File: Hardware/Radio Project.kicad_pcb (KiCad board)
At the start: 10 copper layers, 100 x 70 mm, 88 parts, among them J1 132225, J2 132225, J3 USB_C_Receptacle, J4 FTSH-105-X-X-DV-007-P-X, J5 WE-RJ45_7499010211A, SW1 208-4, U1 STM32F407VGT6, U2 ADP2164ACPZ-3.3-R7, U3 Si4464, U4 Si4464, U5 DP83822IRHBR

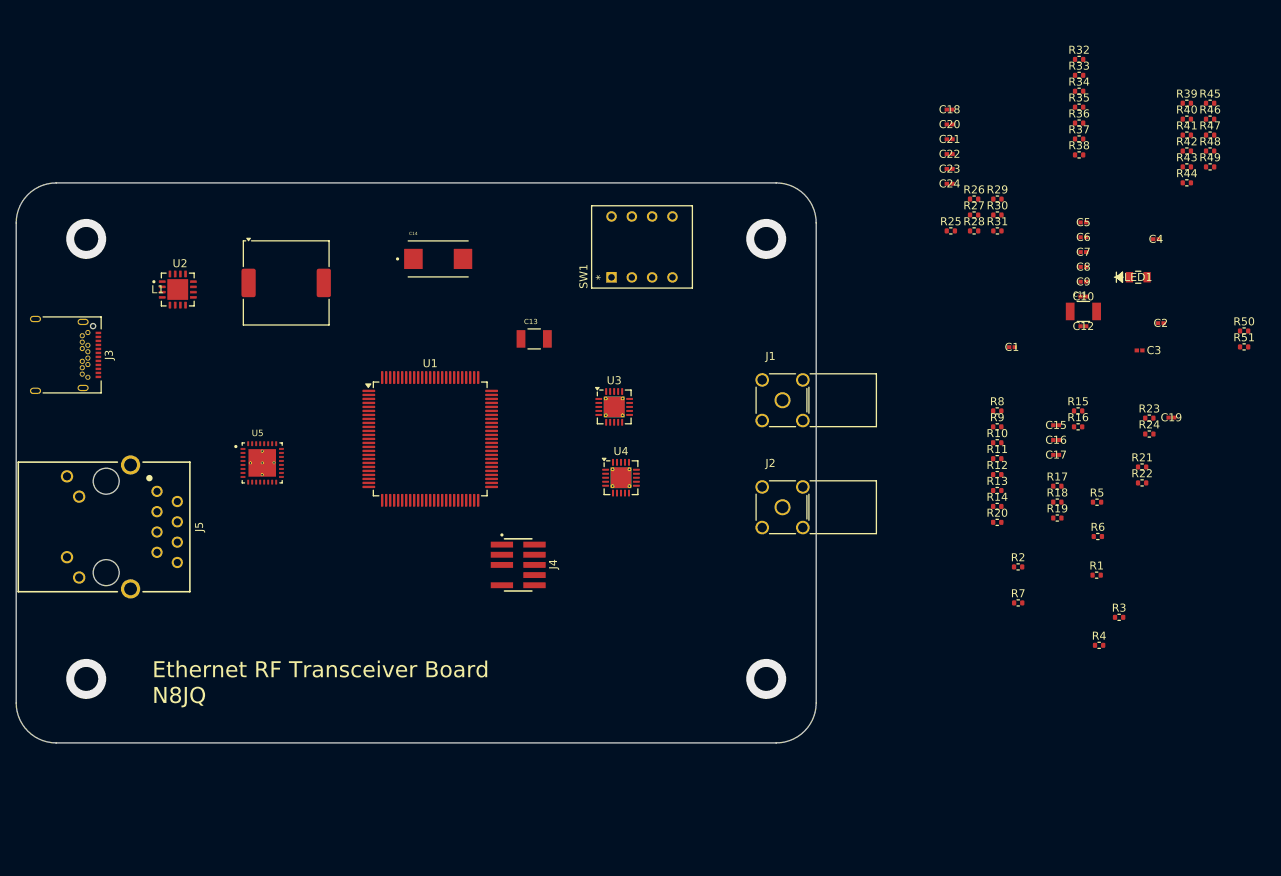
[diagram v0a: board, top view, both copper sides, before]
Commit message: Added oscillators, reset button, and finalized ETH connection
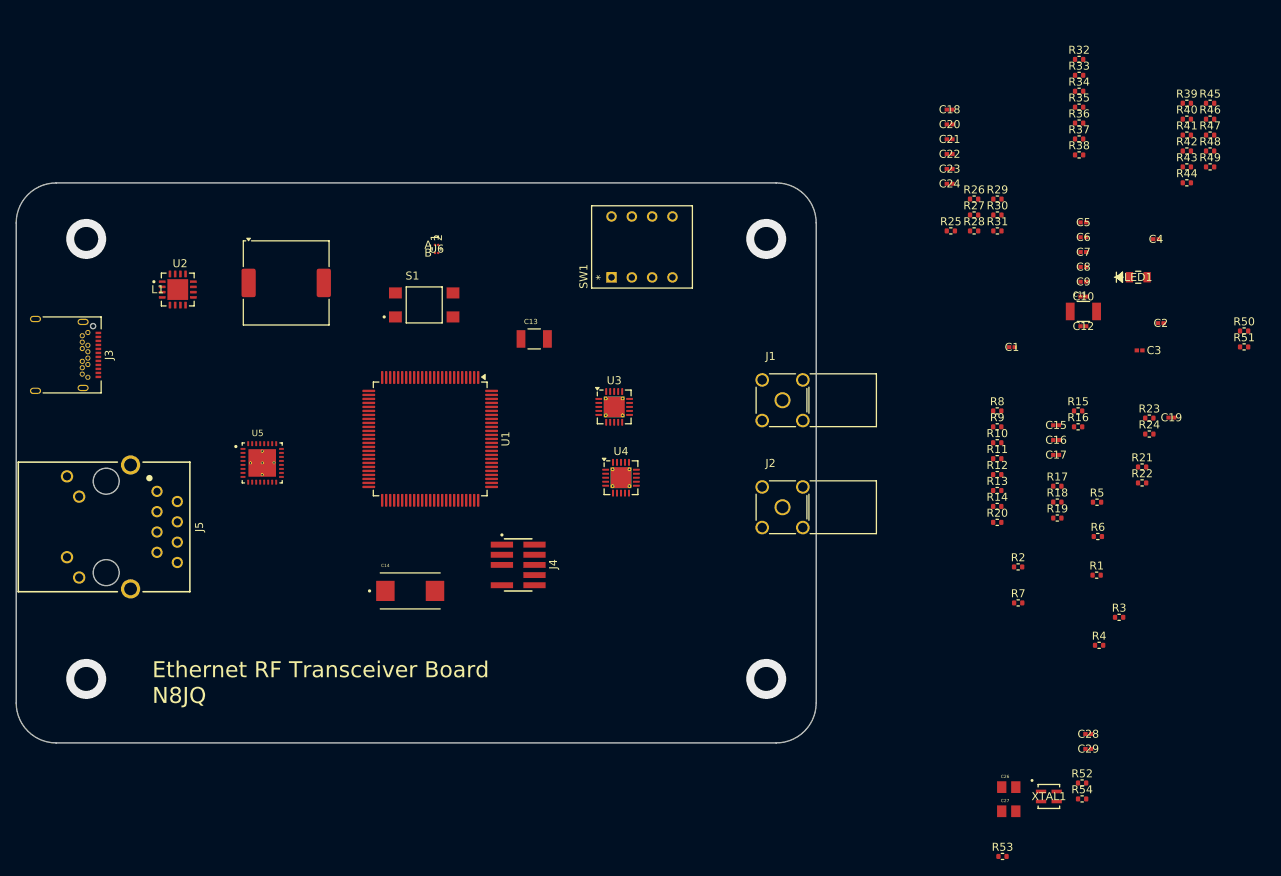
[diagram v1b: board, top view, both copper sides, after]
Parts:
- added C26: 2.2uF, 0805ZC225KAT2A:CAPC2012X140N, F.Cu at (220.3, 123.5)
- added C27: 2.2uF, 0805ZC225KAT2A:CAPC2012X140N, F.Cu at (220.3, 126.5)
- added C28: 100nF, C0402C104J8RACTU:CAPC10555_55N_KEM-L, F.Cu at (230.3, 116.9)
- added C29: 100nF, C0402C104J8RACTU:CAPC10555_55N_KEM-L, F.Cu at (230.3, 118.7)
- added R52: 40, Resistor_SMD:R_0402_1005Metric, F.Cu at (229.5, 123.0)
- added R53: 40, Resistor_SMD:R_0402_1005Metric, F.Cu at (219.5, 132.2)
- added R54: 40, Resistor_SMD:R_0402_1005Metric, F.Cu at (229.5, 125.0)
- added S1: TL3305AF160QG, TL3305AF160QG:SW_TL3305AF160QG, F.Cu at (147.2, 63.2)
- added U6: SIT1566AC-JV-XXE-32.768D, SIT1566AC_JV_XXE_32_768D:BGA_E-32.768D_SIT, F.Cu at (148.8, 56.3)
- added XTAL1: SIT5000AICGE-25MHz, SIT5000AICGE_33N0_25_000000Y:SIT5000_2.7x2.4_SIT-M, F.Cu at (225.3, 124.7)
- R50, R51: value 4.7k -> 5.1k
- moved C14 41.6 mm to (145.5, 99.0)
- turned U1 to -90 degrees
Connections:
- R50 pad 1: +3.3V -> Net-(J3-CC2)
- R50 pad 2: Net-(J3-CC1) -> GND
- R51 pad 1: +3.3V -> Net-(J3-CC1)
- R51 pad 2: Net-(J3-CC2) -> GND
- U1 pad 12: unconnected-(U1-PH0-Pad12) -> CLK_25MHZ
- U1 pad 15: unconnected-(U1-PC0-Pad15) -> Net-(U1-PC0)
- U1 pad 27: GND -> Net-(U1-VSS-Pad27)
- U1 pad 49: unconnected-(U1-VCAP_1-Pad49) -> Net-(U1-VCAP_1)
- U1 pad 63: unconnected-(U1-PC6-Pad63) -> Net-(U1-PC6)
- U1 pad 73: unconnected-(U1-VCAP_2-Pad73) -> Net-(U1-VCAP_2)
- U1 pad 74: GND -> Net-(U1-VSS-Pad27)
- U1 pad 8: unconnected-(U1-PC14-Pad8) -> Net-(U1-PC14)
- U1 pad 99: GND -> Net-(U1-VSS-Pad27)
- U5 pad 18: unconnected-(U5-~{RESET}-Pad18) -> ETH_RESET
- U5 pad 8: unconnected-(U5-~{INT}/PWDN-Pad8) -> Net-(U5-~{INT}/PWDN)

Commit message: changed to SI4468, added 30 MHz oscillators, and connected it to MCU
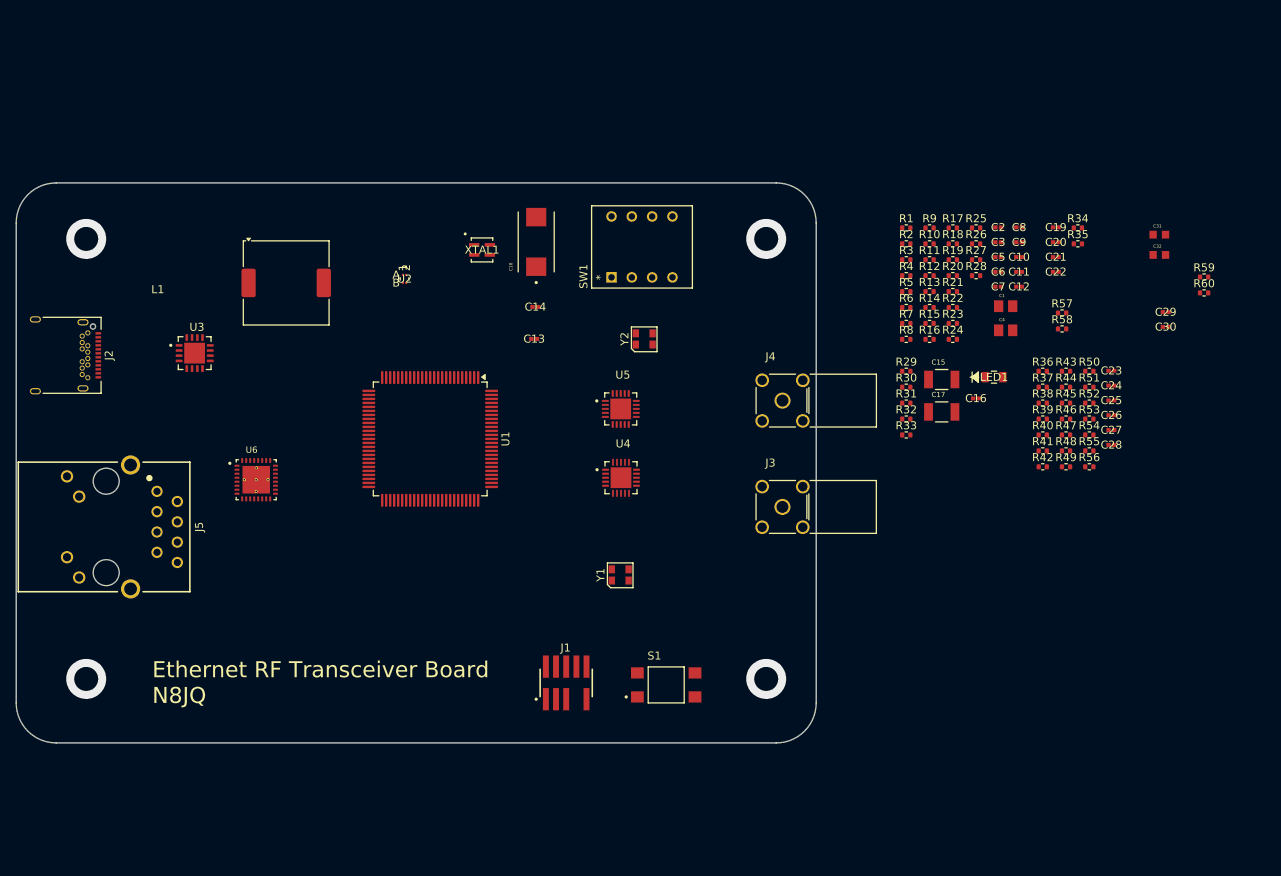
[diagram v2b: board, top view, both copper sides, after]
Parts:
- added C25: 100nF, C0402C104J8RACTU:CAPC10555_55N_KEM-L, F.Cu at (233.1, 75.2)
- added C30: 100nF, C0402C104J8RACTU:CAPC10555_55N_KEM-L, F.Cu at (239.9, 66.0)
- added C31: 100 pF, 0603ZA101FAT2A:CAPC1608X90N, F.Cu at (239.1, 54.5)
- added C32: 100 pF, 0603ZA101FAT2A:CAPC1608X90N, F.Cu at (239.1, 57.0)
- added R55: 49.9, Resistor_SMD:R_0402_1005Metric, F.Cu at (230.4, 81.5)
- added R56: 49.9, Resistor_SMD:R_0402_1005Metric, F.Cu at (230.4, 83.5)
- added R57: 40, Resistor_SMD:R_0402_1005Metric, F.Cu at (227.0, 64.3)
- added R58: 40, Resistor_SMD:R_0402_1005Metric, F.Cu at (227.0, 66.2)
- added R59: 40, Resistor_SMD:R_0402_1005Metric, F.Cu at (244.7, 59.8)
- added R60: 40, Resistor_SMD:R_0402_1005Metric, F.Cu at (244.7, 61.8)
- added Y1: TG2520SMN 30.0000M-MCGNNM0, TG2520SMN:TG2520SMN, F.Cu at (171.8, 97.0)
- added Y2: TG2520SMN 30.0000M-MCGNNM0, TG2520SMN:TG2520SMN, F.Cu at (174.8, 67.5)
- C1, C4: value 100nF -> 2.2uF; footprint C0402C104J8RACTU:CAPC10555_55N_KEM-L -> 0805ZC225KAT2A:CAPC2012X140N
- C11: value 47uF -> 100nF; footprint C3225X5R0J476M250AA:CAP_C3225X5R0J476M250AA -> C0402C104J8RACTU:CAPC10555_55N_KEM-L
- C13: value 100uF -> 100nF; footprint C3225X5R0J107M250AB:CAP_C3225X5R0J107M250AB -> C0402C104J8RACTU:CAPC10555_55N_KEM-L
- C14: value 330uF -> 100nF; footprint TRME337K010R0035:CAPPM7343X310N -> C0402C104J8RACTU:CAPC10555_55N_KEM-L
- C15: value 100nF -> 47uF; footprint C0402C104J8RACTU:CAPC10555_55N_KEM-L -> C3225X5R0J476M250AA:CAP_C3225X5R0J476M250AA
- C17: value 100nF -> 100uF; footprint C0402C104J8RACTU:CAPC10555_55N_KEM-L -> C3225X5R0J107M250AB:CAP_C3225X5R0J107M250AB
- C18: value 100nF -> 330uF; footprint C0402C104J8RACTU:CAPC10555_55N_KEM-L -> TRME337K010R0035:CAPPM7343X310N
- C26, C27: value 2.2uF -> 100nF; footprint 0805ZC225KAT2A:CAPC2012X140N -> C0402C104J8RACTU:CAPC10555_55N_KEM-L
- J1: value 132225 -> FTSH-105-X-X-DV-007-P-X; footprint 132225:CONN_132225_AMP -> FTSH-105-01-L-DV-007-K:SAMTEC_FTSH-105-X-X-DV-007-P-X
- J2: value 132225 -> USB_C_Receptacle; footprint 132225:CONN_132225_AMP -> Connector_USB:USB_C_Receptacle_Amphenol_12401548E4-2A
- J3: value USB_C_Receptacle -> 132225; footprint Connector_USB:USB_C_Receptacle_Amphenol_12401548E4-2A -> 132225:CONN_132225_AMP
- J4: value FTSH-105-X-X-DV-007-P-X -> 132225; footprint FTSH-105-01-L-DV-007-K:SAMTEC_FTSH-105-X-X-DV-007-P-X -> 132225:CONN_132225_AMP
- R18, R19: value 100k -> 40
- R20, R21: value 1K -> 40
- R22: value 10 -> 100k
- R23: value 10k -> 100k
- R24: value 60 -> 40
- R27, R28: value 40 -> 1K
- R29: value 40 -> 10
- R30: value 4.87k -> 10k
- R31, R32: value 40 -> 5.1k
- R33: value 40 -> 60
- R36: value 40 -> 4.87k
- R42, R43, R44, R45, R48: value 49.9 -> 40
- R46, R47: value 2.49k -> 40
- R50, R51: value 5.1k -> 49.9
- R52: value 40 -> 49.9
- R53, R54: value 40 -> 2.49k
- U2: value ADP2164ACPZ-3.3-R7 -> SIT1566AC-JV-XXE-32.768D; footprint ADP2164ACPZ_3_3_R7:QFN65P400X400X80-17N -> SIT1566AC_JV_XXE_32_768D:BGA_E-32.768D_SIT
- U3: value Si4464 -> ADP2164ACPZ-3.3-R7; footprint Package_DFN_QFN:QFN-20-1EP_4x4mm_P0.5mm_EP2.6x2.6mm_ThermalVias -> ADP2164ACPZ_3_3_R7:QFN65P400X400X80-17N
- U4: value Si4464 -> SI4468-A2A-IM; footprint Package_DFN_QFN:QFN-20-1EP_4x4mm_P0.5mm_EP2.6x2.6mm_ThermalVias -> SI4468_A2A_IM:QFN50P400X400X90-21N
- U5: value DP83822IRHBR -> SI4468-A2A-IM; footprint DP83822IRHBR:IC_DP83822IRHBR -> SI4468_A2A_IM:QFN50P400X400X90-21N
- U6: value SIT1566AC-JV-XXE-32.768D -> DP83822IRHBR; footprint SIT1566AC_JV_XXE_32_768D:BGA_E-32.768D_SIT -> DP83822IRHBR:IC_DP83822IRHBR
- moved XTAL1 98.4 mm to (154.5, 56.4)
- moved J2 92.5 mm to (101.5, 69.5)
- moved J3 92.5 mm to (192.0, 88.5)
- moved S1 56.3 mm to (177.5, 110.8)
- moved R53 55.7 mm to (230.4, 77.5)
- moved C29 55.5 mm to (239.9, 64.1)
- moved C18 54.3 mm to (161.2, 55.4), turned to 90 degrees
- moved U3 52.9 mm to (118.6, 69.3)
- moved R4 52.1 mm to (207.5, 59.6)
- moved R3 52.0 mm to (207.5, 57.6)
- moved R33 49.9 mm to (207.5, 79.5)
- moved R32 49.9 mm to (207.5, 77.5)
- moved R1 49.5 mm to (207.5, 53.6)
- moved C27 49.3 mm to (233.1, 78.9)
- moved C26 48.2 mm to (233.1, 77.0)
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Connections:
- C1 pad 1: NRST -> GND
- C1 pad 2: GND -> Net-(U1-VCAP_1)
- C11 pad 1: +5V -> +3.3V
- C12 pad 1: Net-(U2-EN) -> Net-(U2-Vdd)
- C15 pad 1: +3.3V -> +5V
- C16 pad 1: +3.3V -> Net-(U3-EN)
- C2 pad 1: +3.3V -> NRST
- C21 pad 1: Net-(C21-Pad1) -> +3.3V
- C22 pad 1: Net-(C22-Pad1) -> +3.3V
- C26 pad 1: GND -> Net-(C26-Pad1)
- C26 pad 2: Net-(U1-VCAP_2) -> GND
- C27 pad 1: GND -> +3.3V
- C27 pad 2: Net-(U1-VCAP_1) -> GND
- C28 pad 1: Net-(U6-Vdd) -> +3.3V
- C4 pad 1: +3.3V -> GND
- C4 pad 2: GND -> Net-(U1-VCAP_2)
- L1 pad 1: Net-(U2-SW) -> Net-(U3-SW)
- R10 pad 1: ETH_TXD3 -> RF1_SDI
- R10 pad 2: Net-(U1-PB8) -> Net-(U1-PB5)
- R11 pad 1: ETH_TX_EN -> ETH_TXD3
- R11 pad 2: Net-(U1-PB11) -> Net-(U1-PB8)
- R12 pad 1: ETH_TXD0 -> ETH_TX_EN
- R12 pad 2: Net-(U1-PB12) -> Net-(U1-PB11)
- R13 pad 1: ETH_TXD1 -> ETH_TXD0
- R13 pad 2: Net-(U1-PB13) -> Net-(U1-PB12)
- R14 pad 1: ETH_MDC -> ETH_TXD1
- R14 pad 2: Net-(U1-PC1) -> Net-(U1-PB13)
- R15 pad 1: ETH_TXD2 -> ETH_RESET
- R15 pad 2: Net-(U1-PC2) -> Net-(U1-PC0)
- R16 pad 1: RF2_SCLK -> ETH_MDC
- R16 pad 2: Net-(U1-PC10) -> Net-(U1-PC1)
- R17 pad 1: RF2_SDI -> ETH_TXD2
- R17 pad 2: Net-(U1-PC12) -> Net-(U1-PC2)
- R18 pad 1: +3.3V -> ETH_INT_PWDN
- R18 pad 2: Boot1 -> Net-(U1-PC6)
- R19 pad 1: +3.3V -> RF2_SCLK
- R19 pad 2: Boot0 -> Net-(U1-PC10)
- R20 pad 1: Net-(R20-Pad1) -> RF2_SDI
- R20 pad 2: GND -> Net-(U1-PC12)
- R21 pad 1: Net-(R21-Pad1) -> CLK_25MHZ
- R21 pad 2: GND -> Net-(XTAL1-CLK)
- R22 pad 1: +5V -> +3.3V
- R22 pad 2: Net-(U2-EN) -> Boot1
- R23 pad 1: Net-(U2-EN) -> +3.3V
- R23 pad 2: Net-(U2-PGOOD) -> Boot0
- R24 pad 1: GND -> SWDIO
- R24 pad 2: Net-(LED1-Pad1) -> Net-(J1-Pad02)
- R25 pad 1: Net-(U3-SDO) -> SWDCLK
- R25 pad 2: RF1_SDO -> Net-(J1-Pad04)
- R26 pad 1: Net-(U4-SDO) -> NRST
- R26 pad 2: RF2_SDO -> Net-(J1-Pad10)
- R27 pad 1: SWDIO -> Net-(R27-Pad1)
- R27 pad 2: Net-(J4-Pad02) -> GND
- R28 pad 1: SWDCLK -> Net-(R28-Pad1)
- R28 pad 2: Net-(J4-Pad04) -> GND
- R29 pad 1: NRST -> +5V
- R29 pad 2: Net-(J4-Pad10) -> Net-(U3-EN)
- R3 pad 1: RF2_NSS -> Net-(U2-CLK_Out)
- R3 pad 2: Net-(U1-PA4) -> CLK_32KHz
- R30 pad 1: GND -> Net-(U3-EN)
- R30 pad 2: Net-(U5-RBIAS) -> Net-(U3-PGOOD)
- R31 pad 1: Net-(U5-TX_CLK) -> Net-(J2-CC2)
- R31 pad 2: CLK_ETH_TX -> GND
- R32 pad 1: Net-(U5-RX_CLK) -> Net-(J2-CC1)
- R32 pad 2: CLK_ETH_RX -> GND
- R33 pad 1: Net-(U5-MDIO) -> GND
- R33 pad 2: ETH_MDIO -> Net-(LED1-Pad1)
- R34 pad 1: Net-(U5-RX_D3/GPIO3) -> Net-(U4-SDO)
- R34 pad 2: ETH_RX_D3 -> RF1_SDO
- R35 pad 1: Net-(U5-RX_D2) -> Net-(U5-SDO)
- R35 pad 2: ETH_RX_D2 -> RF2_SDO
- R36 pad 1: Net-(U5-RX_D1) -> GND
- R36 pad 2: ETH_RX_D1 -> Net-(U6-RBIAS)
- R37 pad 1: Net-(U5-RX_D0) -> Net-(U6-~{INT}/PWDN)
- R37 pad 2: ETH_RX_D0 -> ETH_INT_PWDN
- R38 pad 1: Net-(U5-RX_DV/RX_CTRL) -> Net-(U6-TX_CLK)
- R38 pad 2: ETH_RX_DV -> CLK_ETH_TX
- R39 pad 1: Net-(U5-RX_ER) -> Net-(U6-RX_CLK)
- R39 pad 2: ETH_RX_ER -> CLK_ETH_RX
- R4 pad 1: RF1_SCLK -> RF2_NSS
- R4 pad 2: Net-(U1-PA5) -> Net-(U1-PA4)
- R40 pad 1: Net-(U5-CRS/CRS_DV) -> Net-(U6-MDIO)
- R40 pad 2: ETH_RX_CRS -> ETH_MDIO
- R41 pad 1: Net-(U5-COL/GPIO2) -> Net-(U6-RX_D3/GPIO3)
- R41 pad 2: ETH_RX_COL -> ETH_RX_D3
- R42 pad 1: Net-(C21-Pad1) -> Net-(U6-RX_D2)
- R42 pad 2: Net-(J5-RD+) -> ETH_RX_D2
- R43 pad 1: Net-(J5-RD-) -> Net-(U6-RX_D1)
- R43 pad 2: Net-(C21-Pad1) -> ETH_RX_D1
- R44 pad 1: Net-(C22-Pad1) -> Net-(U6-RX_D0)
- R44 pad 2: Net-(J5-TD+) -> ETH_RX_D0
- R45 pad 1: Net-(J5-TD-) -> Net-(U6-RX_DV/RX_CTRL)
- R45 pad 2: Net-(C22-Pad1) -> ETH_RX_DV
- R46 pad 1: GND -> Net-(U6-RX_ER)
- R46 pad 2: LED_0 -> ETH_RX_ER
- R47 pad 1: GND -> Net-(U6-CRS/CRS_DV)
- R47 pad 2: LED_1 -> ETH_RX_CRS
- R48 pad 1: GND -> Net-(U6-COL/GPIO2)
- R48 pad 2: Net-(J5-Pad11) -> ETH_RX_COL
- R49 pad 1: GND -> Net-(C25-Pad1)
- R49 pad 2: Net-(J5-Pad10) -> Net-(J5-RD+)
- R5 pad 1: CLK_25MHZ_MCO -> RF1_SCLK
- R5 pad 2: Net-(U1-PA8) -> Net-(U1-PA5)
- R50 pad 1: Net-(J3-CC2) -> Net-(J5-RD-)
- R50 pad 2: GND -> Net-(C25-Pad1)
- R51 pad 1: Net-(J3-CC1) -> Net-(C26-Pad1)
- R51 pad 2: GND -> Net-(J5-TD+)
- R52 pad 1: ETH_RESET -> Net-(J5-TD-)
- R52 pad 2: Net-(U1-PC0) -> Net-(C26-Pad1)
- R53 pad 1: Net-(U5-~{INT}/PWDN) -> GND
- R53 pad 2: ETH_INT_PWDN -> LED_0
- R54 pad 1: ETH_INT_PWDN -> GND
- R54 pad 2: Net-(U1-PC6) -> LED_1
- R6 pad 1: SWDIO -> CLK_25MHZ_MCO
- R6 pad 2: Net-(U1-PA13) -> Net-(U1-PA8)
- R7 pad 1: RF1_NSS -> SWDIO
- R7 pad 2: Net-(U1-PA15) -> Net-(U1-PA13)
- R8 pad 1: SWO -> RF1_NSS
- R8 pad 2: Net-(U1-PB3) -> Net-(U1-PA15)
- R9 pad 1: RF1_SDI -> SWO
- R9 pad 2: Net-(U1-PB5) -> Net-(U1-PB3)
- SW1 pad 5: Net-(R21-Pad1) -> Net-(R28-Pad1)
- SW1 pad 6: Net-(R20-Pad1) -> Net-(R27-Pad1)
- U1 pad 47: unconnected-(U1-PB10-Pad47) -> ETH_RX_ER
- U1 pad 8: Net-(U1-PC14) -> CLK_32KHz
- U2 pad 1: Net-(U2-EN) -> unconnected-(U2-NC-Pad1)
- U2 pad 2: Net-(U2-EN) -> Net-(U2-CLK_Out)
- U2 pad 3: Net-(U2-EN) -> Net-(U2-Vdd)
- U2 pad 4: +3.3V -> GND
- U3 pad 1: RF1_SDN -> Net-(U3-EN)
- U3 pad 10: unconnected-(U3-GPIO1-Pad10) -> Net-(U3-SW)
- U3 pad 11: unconnected-(U3-~{IRQ}-Pad11) -> Net-(U3-SW)
- U3 pad 12: RF1_SCLK -> +5V
- U3 pad 13: Net-(U3-SDO) -> +5V
- U3 pad 14: RF1_SDI -> Net-(U3-EN)
- U3 pad 15: RF1_NSS -> Net-(U3-EN)
- U3 pad 16: unconnected-(U3-XOUT-Pad16) -> Net-(U3-PGOOD)
- U3 pad 17: unconnected-(U3-XIN-Pad17) -> GND
- U3 pad 2: unconnected-(U3-RXp-Pad2) -> Net-(U3-EN)
- U3 pad 3: unconnected-(U3-RXn-Pad3) -> Net-(U3-EN)
- U3 pad 4: unconnected-(U3-TX-Pad4) -> +3.3V
- U3 pad 5: unconnected-(U3-NC-Pad5) -> GND
- U3 pad 6: +3.3V -> GND
- U3 pad 7: unconnected-(U3-TXRAMP-Pad7) -> GND
- U3 pad 8: +3.3V -> GND
- U3 pad 9: unconnected-(U3-GPIO0-Pad9) -> Net-(U3-SW)
- U4 pad 1: RF2_SDN -> RF1_SDN
- U4 pad 11: unconnected-(U4-~{IRQ}-Pad11) -> Net-(U4-NIRQ)
- U4 pad 12: RF2_SCLK -> RF1_SCLK
- U4 pad 14: RF2_SDI -> RF1_SDI
- U4 pad 15: RF2_NSS -> RF1_NSS
- U4 pad 17: unconnected-(U4-XIN-Pad17) -> Net-(U4-XIN)
- U4 pad 5: unconnected-(U4-NC-Pad5) -> (no net)
- U5 pad 1: Net-(U5-RX_D3/GPIO3) -> RF2_SDN
- U5 pad 10: Net-(J5-RD+) -> unconnected-(U5-GPIO1-Pad10)
- U5 pad 11: Net-(J5-TD-) -> Net-(U5-NIRQ)
- U5 pad 12: Net-(J5-TD+) -> RF2_SCLK
- U5 pad 13: unconnected-(U5-NC_13-Pad13) -> Net-(U5-SDO)
- U5 pad 14: +3.3V -> RF2_SDI
- U5 pad 15: unconnected-(U5-NC_15-Pad15) -> RF2_NSS
- U5 pad 16: Net-(U5-RBIAS) -> unconnected-(U5-XOUT-Pad16)
- U5 pad 17: LED_0 -> Net-(U5-XIN)
- U5 pad 18: ETH_RESET -> GND
- U5 pad 19: Net-(U5-MDIO) -> unconnected-(U5-GPIO2-Pad19)
- U5 pad 2: Net-(U5-TX_CLK) -> unconnected-(U5-RXP-Pad2)
- U5 pad 20: ETH_MDC -> unconnected-(U5-GPIO3-Pad20)
- U5 pad 21: +3.3V -> GND
- U5 pad 3: ETH_TX_EN -> unconnected-(U5-RXN-Pad3)
- U5 pad 4: ETH_TXD0 -> unconnected-(U5-TX-Pad4)
- U5 pad 5: ETH_TXD1 -> (no net)
- U5 pad 6: ETH_TXD2 -> +3.3V
- U5 pad 7: ETH_TXD3 -> unconnected-(U5-TXRAMP-Pad7)
- U5 pad 8: Net-(U5-~{INT}/PWDN) -> +3.3V
- U5 pad 9: Net-(J5-RD-) -> unconnected-(U5-GPIO0-Pad9)
- U6 pad 1: unconnected-(U6-NC-Pad1) -> Net-(U6-RX_D3/GPIO3)
- U6 pad 2: Net-(U1-PC14) -> Net-(U6-TX_CLK)
- U6 pad 3: Net-(U6-Vdd) -> ETH_TX_EN
- U6 pad 4: GND -> ETH_TXD0
- XTAL1 pad 3: CLK_25MHZ -> Net-(XTAL1-CLK)

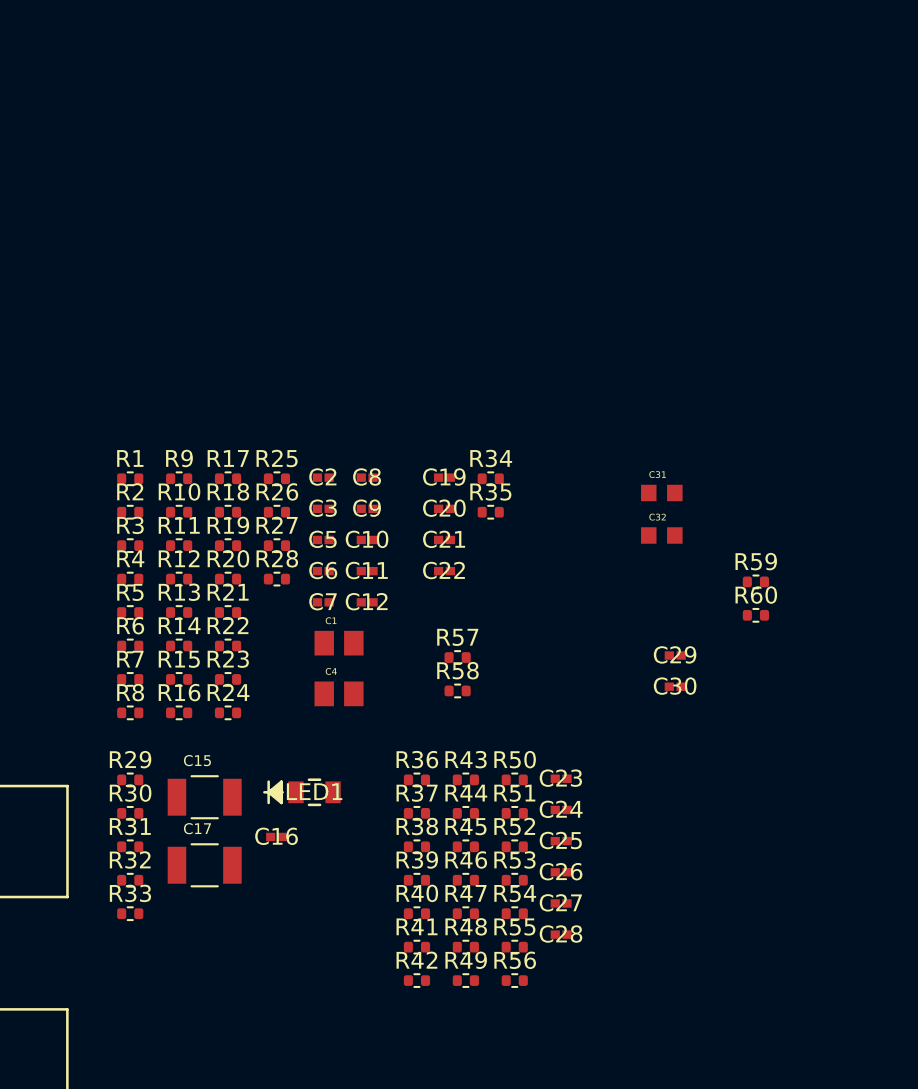
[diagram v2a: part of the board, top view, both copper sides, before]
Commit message: fixed incorrect naming on RF clk and connected RF NIRQ lines
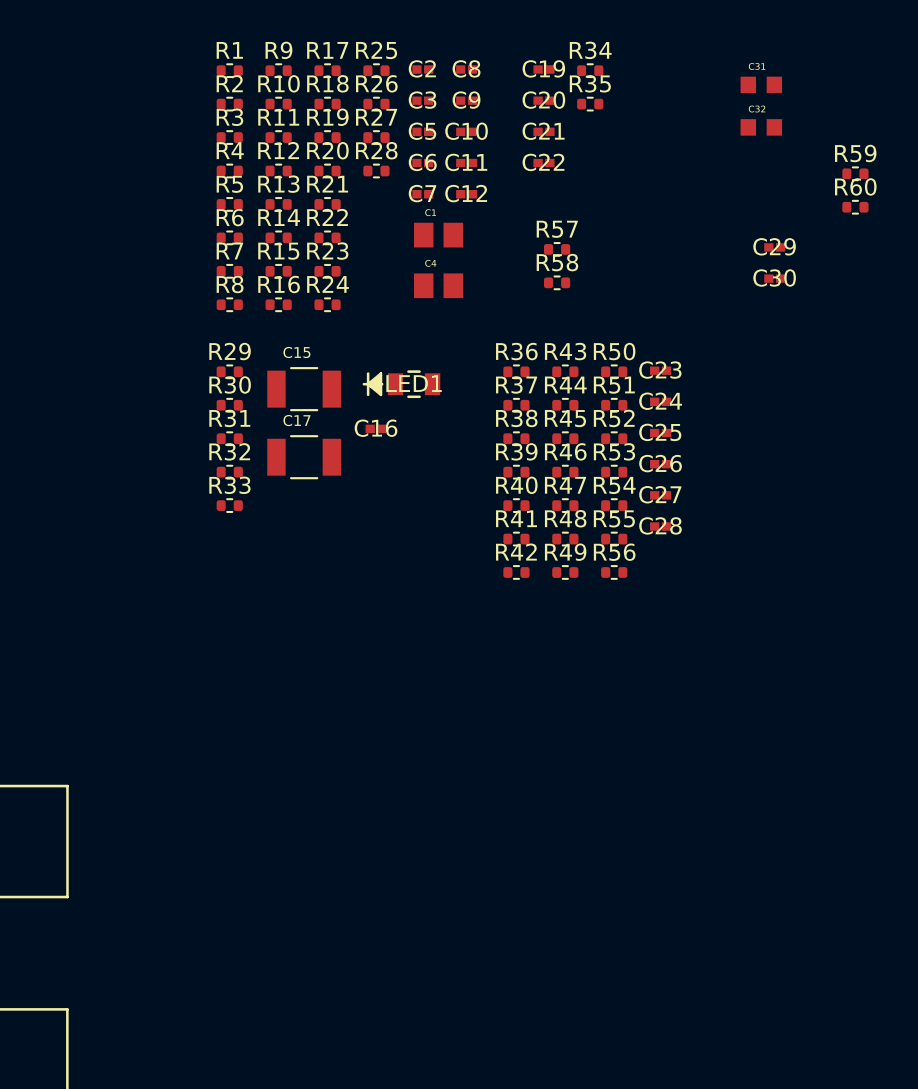
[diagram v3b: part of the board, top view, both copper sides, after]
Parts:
- moved C24 25.0 mm to (239.1, 49.0)
- moved C25 25.0 mm to (239.1, 50.9)
- moved LED1 25.0 mm to (224.4, 48.0)
- moved R33 25.0 mm to (213.4, 55.2)
- moved R40 25.0 mm to (230.5, 55.2)
- moved R47 25.0 mm to (233.4, 55.2)
- moved R54 25.0 mm to (236.3, 55.2)
- moved R57 25.0 mm to (232.9, 40.0)
- moved C15 25.0 mm to (217.9, 48.3)
- moved C20 25.0 mm to (232.1, 31.1)
- moved C3 25.0 mm to (224.9, 31.1)
- moved C9 25.0 mm to (227.5, 31.1)
- moved C1 25.0 mm to (225.9, 39.1)
- moved C10 25.0 mm to (227.5, 33.0)
- moved C11 25.0 mm to (227.5, 34.8)
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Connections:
- C31 pad 2: CLK_RF2_30MHz -> CLK_RF1_30MHz
- C32 pad 2: CLK_RF1_30MHz -> CLK_RF2_30MHz
- R58 pad 2: RF1_NIRQ -> RF2_NIRQ
- U1 pad 64: unconnected-(U1-PC7-Pad64) -> RF1_NIRQ
- U1 pad 65: unconnected-(U1-PC8-Pad65) -> RF2_NIRQ
